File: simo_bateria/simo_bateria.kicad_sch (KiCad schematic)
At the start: 16 parts, among them J1 BAT_LEVEL, J2 Plugin, J3 VBAT IN, J4 SWD, SW1 SW_Reed, U1 mod_mt3608, U2 BSS314PEH6327XTSA1

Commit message: UPDATE
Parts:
- removed R1: 355k, Resistor_THT:R_Axial_DIN0309_L9.0mm_D3.2mm_P15.24mm_Horizontal, symbol Device:R
- removed R2: 155k, Resistor_THT:R_Axial_DIN0309_L9.0mm_D3.2mm_P15.24mm_Horizontal, symbol Device:R
- removed R3: 10k, Resistor_THT:R_Axial_DIN0309_L9.0mm_D3.2mm_P15.24mm_Horizontal, symbol Device:R
- added R1: 10k, simo_bateria:RESITOR_THT, symbol simo_bateria:R
- added R2: 355k, simo_bateria:RESITOR_THT, symbol simo_bateria:R
- added R3: 155k, simo_bateria:RESITOR_THT, symbol simo_bateria:R
- SW1: footprint Resistor_THT:R_Axial_DIN0309_L9.0mm_D3.2mm_P15.24mm_Horizontal -> simo_bateria:RESITOR_THT
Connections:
- net at J1.2 (Pin_2): now also R2.1, R3.1
- net at J1.1 (Pin_1): now also R3.2
- net at J3.1 (Pin_1), J4.1 (Pin_1), SW1.1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: now also R2.2
- net at J4.2 (Pin_2), SW1.2, U2.1: now also R1.1
- net at J3.2 (Pin_2), U1.2 (VIN-): now also R1.2
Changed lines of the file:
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@@
+    (stroke (width 0) (type default) (color 0 0 0 0))
+  )
+  (wire (pts (xy 153.67 127) (xy 191.77 127))
     (stroke (width 0) (type default) (color 0 0 0 0))
   )
@@
   )
   (wire (pts (xy 191.77 127) (xy 191.77 128.27))
-    (stroke (width 0) (type default) (color 0 0 0 0))
-  )
-  (wire (pts (xy 153.67 127) (xy 191.77 127))
     (stroke (width 0) (type default) (color 0 0 0 0))
   )
@@
     )
   )
-  (symbol (lib_id "Device:R") (at 214.63 76.2 0) (mirror y) (unit 1)
-    (in_bom yes) (on_board yes) (fields_autoplaced)
-    (property "Reference" "R2" (id 0) (at 212.09 74.9299 0)
-      (effects (font (size 1.27 1.27)) (justify left))
-    )
-    (property "Value" "155k" (id 1) (at 212.09 77.4699 0)
-      (effects (font (size 1.27 1.27)) (justify left))
-    )
-    (property "Footprint" "Resistor_THT:R_Axial_DIN0309_L9.0mm_D3.2mm_P15.24mm_Horizontal" (id 2) (at 216.408 76.2 90)
-      (effects (font (size 1.27 1.27)) hide)
-    )
-    (property "Datasheet" "https://www.seielect.com/Catalog/SEI-CF_CFM.pdf" (id 3) (at 214.63 76.2 0)
-      (effects (font (size 1.27 1.27)) hide)
-    )
-    (pin "1")
-    (pin "2")
-  )
   (symbol (lib_id "simo_bateria:PWR_FLAG") (at 191.77 88.9 0) (unit 1)
     (in_bom yes) (on_board yes) (fields_autoplaced)
@@
     (pin "2")
   )
-  (symbol (lib_id "Device:R") (at 153.67 123.19 0) (unit 1)
-    (in_bom yes) (on_board yes) (fields_autoplaced)
-    (property "Reference" "R3" (id 0) (at 156.21 121.9199 0)
-      (effects (font (size 1.27 1.27)) (justify left))
-    )
-    (property "Value" "10k" (id 1) (at 156.21 124.4599 0)
-      (effects (font (size 1.27 1.27)) (justify left))
-    )
-    (property "Footprint" "Resistor_THT:R_Axial_DIN0309_L9.0mm_D3.2mm_P15.24mm_Horizontal" (id 2) (at 151.892 123.19 90)
-      (effects (font (size 1.27 1.27)) hide)
-    )
-    (property "Datasheet" "https://www.seielect.com/Catalog/SEI-CF_CFM.pdf" (id 3) (at 153.67 123.19 0)
-      (effects (font (size 1.27 1.27)) hide)
-    )
-    (pin "1")
-    (pin "2")
-  )
   (symbol (lib_id "simo_bateria:BSS314PEH6327XTSA1") (at 153.67 118.11 90) (unit 1)
     (in_bom yes) (on_board yes)
@@
       (effects (font (size 1.27 1.27)) (justify left))
     )
-    (property "Footprint" "Resistor_THT:R_Axial_DIN0309_L9.0mm_D3.2mm_P15.24mm_Horizontal" (id 2) (at 140.97 95.25 0)
+    (property "Footprint" "simo_bateria:RESITOR_THT" (id 2) (at 140.97 95.25 0)
       (effects (font (size 1.27 1.27)) hide)
     )
     (property "Datasheet" "https://www.littelfuse.com/~/media/electronics/datasheets/reed_switches/littelfuse_reed_switches_mdsm_4_datasheet.pdf.pdf" (id 3) (at 140.97 95.25 0)
-      (effects (font (size 1.27 1.27)) hide)
-    )
-    (pin "1")
-    (pin "2")
-  )
-  (symbol (lib_id "Device:R") (at 214.63 66.04 0) (mirror y) (unit 1)
-    (in_bom yes) (on_board yes) (fields_autoplaced)
-    (property "Reference" "R1" (id 0) (at 212.09 64.7699 0)
-      (effects (font (size 1.27 1.27)) (justify left))
-    )
-    (property "Value" "355k" (id 1) (at 212.09 67.3099 0)
-      (effects (font (size 1.27 1.27)) (justify left))
-    )
-    (property "Footprint" "Resistor_THT:R_Axial_DIN0309_L9.0mm_D3.2mm_P15.24mm_Horizontal" (id 2) (at 216.408 66.04 90)
-      (effects (font (size 1.27 1.27)) hide)
-    )
-    (property "Datasheet" "https://www.seielect.com/Catalog/SEI-CF_CFM.pdf" (id 3) (at 214.63 66.04 0)
       (effects (font (size 1.27 1.27)) hide)
     )
@@
       (effects (font (size 1.27 1.27)) hide)
     )
-    (property "Datasheet" "" (id 3) (at 207.01 100.33 0)
+    (property "Datasheet" "https://datasheetspdf.com/pdf-file/909246/AEROSEMI/MT3608/1" (id 3) (at 207.01 100.33 0)
       (effects (font (size 1.27 1.27)) hide)
     )
@@
     (pin "4")
   )
+  (symbol (lib_id "simo_bateria:R") (at 214.63 76.2 0) (unit 1)
+    (in_bom yes) (on_board yes) (fields_autoplaced)
+    (property "Reference" "R3" (id 0) (at 217.17 74.9299 0)
+      (effects (font (size 1.27 1.27)) (justify left))
+    )
+    (property "Value" "155k" (id 1) (at 217.17 77.4699 0)
+      (effects (font (size 1.27 1.27)) (justify left))
+    )
+    (property "Footprint" "simo_bateria:RESITOR_THT" (id 2) (at 212.852 76.2 90)
+      (effects (font (size 1.27 1.27)) hide)
+    )
+    (property "Datasheet" "~" (id 3) (at 214.63 76.2 0)
+      (effects (font (size 1.27 1.27)) hide)
+    )
+    (pin "1")
+    (pin "2")
+  )
   (symbol (lib_id "simo_bateria:MountingHole") (at 148.59 176.53 0) (unit 1)
     (in_bom yes) (on_board yes) (fields_autoplaced)
@@
       (effects (font (size 1.27 1.27)) hide)
     )
+  )
+  (symbol (lib_id "simo_bateria:R") (at 153.67 123.19 0) (unit 1)
+    (in_bom yes) (on_board yes) (fields_autoplaced)
+    (property "Reference" "R1" (id 0) (at 156.21 121.9199 0)
+      (effects (font (size 1.27 1.27)) (justify left))
+    )
+    (property "Value" "10k" (id 1) (at 156.21 124.4599 0)
+      (effects (font (size 1.27 1.27)) (justify left))
+    )
+    (property "Footprint" "simo_bateria:RESITOR_THT" (id 2) (at 151.892 123.19 90)
+      (effects (font (size 1.27 1.27)) hide)
+    )
+    (property "Datasheet" "~" (id 3) (at 153.67 123.19 0)
+      (effects (font (size 1.27 1.27)) hide)
+    )
+    (pin "1")
+    (pin "2")
+  )
+  (symbol (lib_id "simo_bateria:R") (at 214.63 66.04 180) (unit 1)
+    (in_bom yes) (on_board yes) (fields_autoplaced)
+    (property "Reference" "R2" (id 0) (at 217.17 64.7699 0)
+      (effects (font (size 1.27 1.27)) (justify right))
+    )
+    (property "Value" "355k" (id 1) (at 217.17 67.3099 0)
+      (effects (font (size 1.27 1.27)) (justify right))
+    )
+    (property "Footprint" "simo_bateria:RESITOR_THT" (id 2) (at 216.408 66.04 90)
+      (effects (font (size 1.27 1.27)) hide)
+    )
+    (property "Datasheet" "~" (id 3) (at 214.63 66.04 0)
+      (effects (font (size 1.27 1.27)) hide)
+    )
+    (pin "1")
+    (pin "2")
   )
   (sheet_instances
@@
       (reference "J4") (unit 1) (value "SWD") (footprint "simo_bateria:JST_EH_B2B-EH-A_1x02_P2.50mm_Vertical")
     )
-    (path "/8da78f3b-5575-47f1-9326-e93636a9e26c"
-      (reference "R1") (unit 1) (value "355k") (footprint "Resistor_THT:R_Axial_DIN0309_L9.0mm_D3.2mm_P15.24mm_Horizontal")
-    )
-    (path "/2a9711d0-b0e4-422e-9cee-c254b4155632"
-      (reference "R2") (unit 1) (value "155k") (footprint "Resistor_THT:R_Axial_DIN0309_L9.0mm_D3.2mm_P15.24mm_Horizontal")
-    )
-    (path "/7042ca4f-e469-455a-96e7-c467adc1a2eb"
-      (reference "R3") (unit 1) (value "10k") (footprint "Resistor_THT:R_Axial_DIN0309_L9.0mm_D3.2mm_P15.24mm_Horizontal")
+    (path "/e4a0a47a-596d-4bad-96f2-1d19d76d15b2"
+      (reference "R1") (unit 1) (value "10k") (footprint "simo_bateria:RESITOR_THT")
+    )
+    (path "/ff283df6-2253-4ab3-b5a6-4bbb6a3cbdd5"
+      (reference "R2") (unit 1) (value "355k") (footprint "simo_bateria:RESITOR_THT")
+    )
+    (path "/d9563f83-41e3-410a-8ad7-e77975d80b10"
+      (reference "R3") (unit 1) (value "155k") (footprint "simo_bateria:RESITOR_THT")
     )
     (path "/791f5746-bb8c-4453-a95c-90ea333e437c"
-      (reference "SW1") (unit 1) (value "SW_Reed") (footprint "Resistor_THT:R_Axial_DIN0309_L9.0mm_D3.2mm_P15.24mm_Horizontal")
+      (reference "SW1") (unit 1) (value "SW_Reed") (footprint "simo_bateria:RESITOR_THT")
     )
     (path "/cfc280ca-e772-47c7-a852-f3ad8b611455"

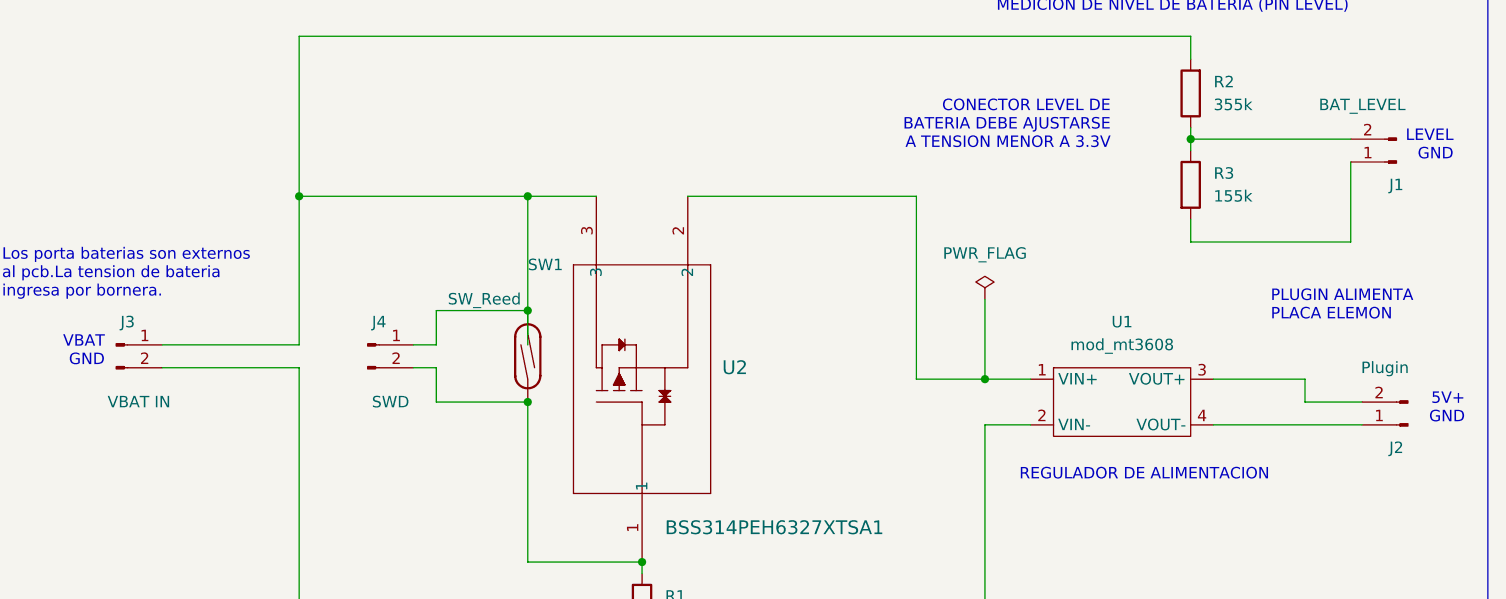
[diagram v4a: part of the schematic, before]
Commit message: [simo_bateria] Se elimino plano de tierra, faltaban archivos por actualizar
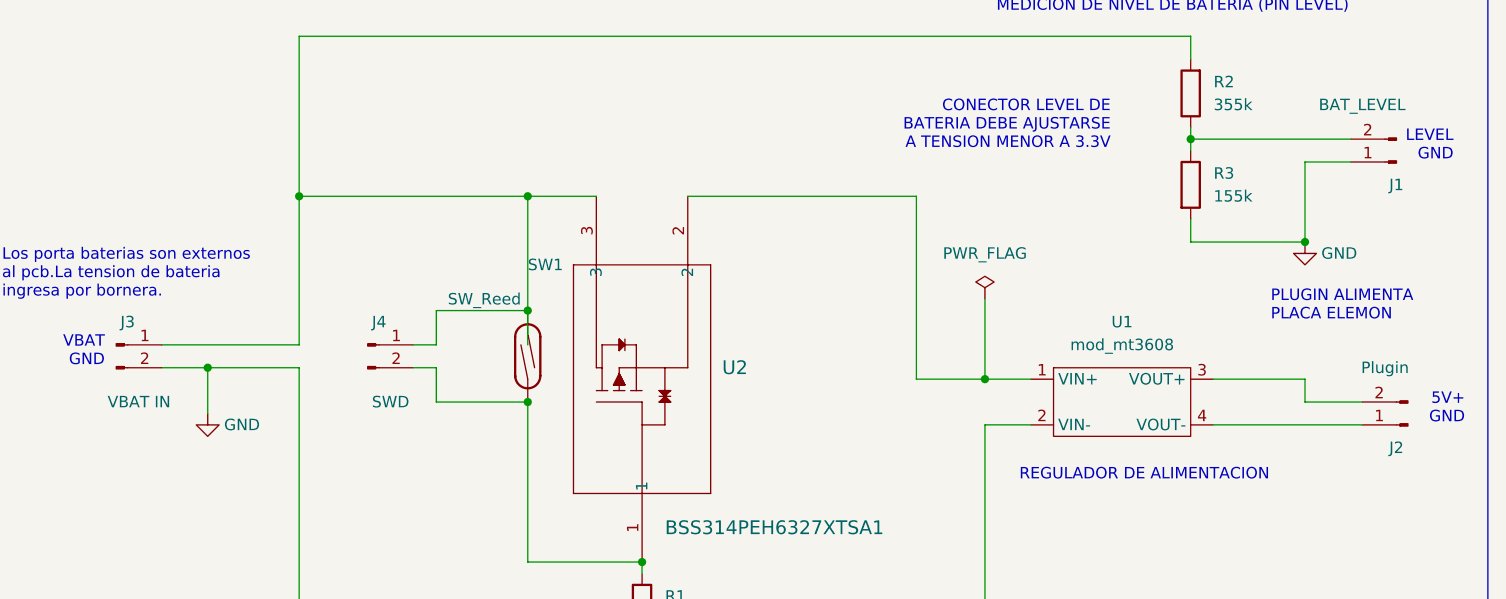
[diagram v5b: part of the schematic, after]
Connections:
- net GND: now reaches J3.2 (Pin_2), R1.2, U1.2 (VIN-)
- net GND: now also J1.1 (Pin_1), R3.2
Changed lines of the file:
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@@
   (junction (at 214.63 71.12) (diameter 0) (color 0 0 0 0)
   )
+  (junction (at 105.41 96.52) (diameter 0) (color 0 0 0 0)
+  )
   (junction (at 140.97 90.17) (diameter 0) (color 0 0 0 0)
   )
@@
   )
   (junction (at 153.67 118.11) (diameter 0) (color 0 0 0 0)
+  )
+  (junction (at 227.33 82.55) (diameter 0) (color 0 0 0 0)
   )
   (junction (at 153.67 127) (diameter 0) (color 0 0 0 0)
@@
     (stroke (width 0) (type default) (color 0 0 0 0))
   )
+  (wire (pts (xy 105.41 96.52) (xy 105.41 101.6))
+    (stroke (width 0) (type default) (color 0 0 0 0))
+  )
   (polyline (pts (xy 247.65 137.16) (xy 53.34 137.16))
     (stroke (width 0) (type default) (color 0 0 0 0))
@@
     (stroke (width 0) (type default) (color 0 0 0 0))
   )
+  (wire (pts (xy 227.33 82.55) (xy 214.63 82.55))
+    (stroke (width 0) (type default) (color 0 0 0 0))
+  )
+  (wire (pts (xy 100.33 96.52) (xy 105.41 96.52))
+    (stroke (width 0) (type default) (color 0 0 0 0))
+  )
+  (wire (pts (xy 105.41 96.52) (xy 115.57 96.52))
+    (stroke (width 0) (type default) (color 0 0 0 0))
+  )
   (wire (pts (xy 115.57 77.47) (xy 140.97 77.47))
     (stroke (width 0) (type default) (color 0 0 0 0))
   )
-  (wire (pts (xy 100.33 96.52) (xy 115.57 96.52))
-    (stroke (width 0) (type default) (color 0 0 0 0))
-  )
   (wire (pts (xy 227.33 100.33) (xy 233.68 100.33))
     (stroke (width 0) (type default) (color 0 0 0 0))
@@
     (stroke (width 0) (type default) (color 0 0 0 0))
   )
-  (wire (pts (xy 232.41 82.55) (xy 214.63 82.55))
-    (stroke (width 0) (type default) (color 0 0 0 0))
-  )
   (wire (pts (xy 130.81 100.33) (xy 140.97 100.33))
     (stroke (width 0) (type default) (color 0 0 0 0))
   )
-  (wire (pts (xy 232.41 73.66) (xy 232.41 82.55))
+  (wire (pts (xy 232.41 73.66) (xy 227.33 73.66))
+    (stroke (width 0) (type default) (color 0 0 0 0))
+  )
+  (wire (pts (xy 227.33 73.66) (xy 227.33 82.55))
     (stroke (width 0) (type default) (color 0 0 0 0))
   )
@@
     (effects (font (size 1.27 1.27)) (justify left bottom))
   )
-  (text "5V+ \nGND\n" (at 245.11 102.87 180)
+  (text " 5V+ \nGND\n" (at 245.11 102.87 180)
     (effects (font (size 1.27 1.27)) (justify right bottom))
   )
@@
       (effects (font (size 1.27 1.27)) hide)
     )
+  )
+  (symbol (lib_id "power:GND") (at 105.41 101.6 0) (unit 1)
+    (in_bom yes) (on_board yes)
+    (property "Reference" "#PWR?" (id 0) (at 105.41 107.95 0)
+      (effects (font (size 1.27 1.27)) hide)
+    )
+    (property "Value" "GND" (id 1) (at 109.22 102.87 0))
+    (property "Footprint" "" (id 2) (at 105.41 101.6 0)
+      (effects (font (size 1.27 1.27)) hide)
+    )
+    (property "Datasheet" "" (id 3) (at 105.41 101.6 0)
+      (effects (font (size 1.27 1.27)) hide)
+    )
+    (pin "1")
   )
   (symbol (lib_id "simo_bateria:Conn_01x02_Male") (at 123.19 93.98 0) (unit 1)
@@
     (pin "2")
   )
+  (symbol (lib_id "power:GND") (at 227.33 82.55 0) (unit 1)
+    (in_bom yes) (on_board yes)
+    (property "Reference" "#PWR?" (id 0) (at 227.33 88.9 0)
+      (effects (font (size 1.27 1.27)) hide)
+    )
+    (property "Value" "GND" (id 1) (at 231.14 83.82 0))
+    (property "Footprint" "" (id 2) (at 227.33 82.55 0)
+      (effects (font (size 1.27 1.27)) hide)
+    )
+    (property "Datasheet" "" (id 3) (at 227.33 82.55 0)
+      (effects (font (size 1.27 1.27)) hide)
+    )
+    (pin "1")
+  )
   (symbol (lib_id "simo_bateria:Conn_01x02_Male") (at 237.49 73.66 180) (unit 1)
     (in_bom yes) (on_board yes)
@@
       (reference "#FLG0102") (unit 1) (value "PWR_FLAG") (footprint "")
     )
+    (path "/3bbefc09-6c5a-48df-b1d7-44dd3eef4f77"
+      (reference "#PWR?") (unit 1) (value "GND") (footprint "")
+    )
+    (path "/b4e9eb92-ce6e-43d1-8449-c34ffd0d9287"
+      (reference "#PWR?") (unit 1) (value "GND") (footprint "")
+    )
     (path "/0e1c8888-24a9-448a-8220-c54ef612d9ed"
